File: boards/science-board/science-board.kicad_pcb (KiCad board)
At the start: 2 copper layers, 93.2 x 93.2 mm, 19 parts, among them J1 Conn_01x02, J10 Conn_01x04, J11 J00-0045NL, J12 Conn_02x03_Counter_Clockwise, J2 Conn_01x08, J3 Conn_01x04, J4 Conn_01x04, J5 Conn_01x08, J6 Conn_01x03, J7 Conn_01x08, J8 Conn_01x08, J9 Conn_01x04, U1 Teensy4.1, U2 LSF0108PWR

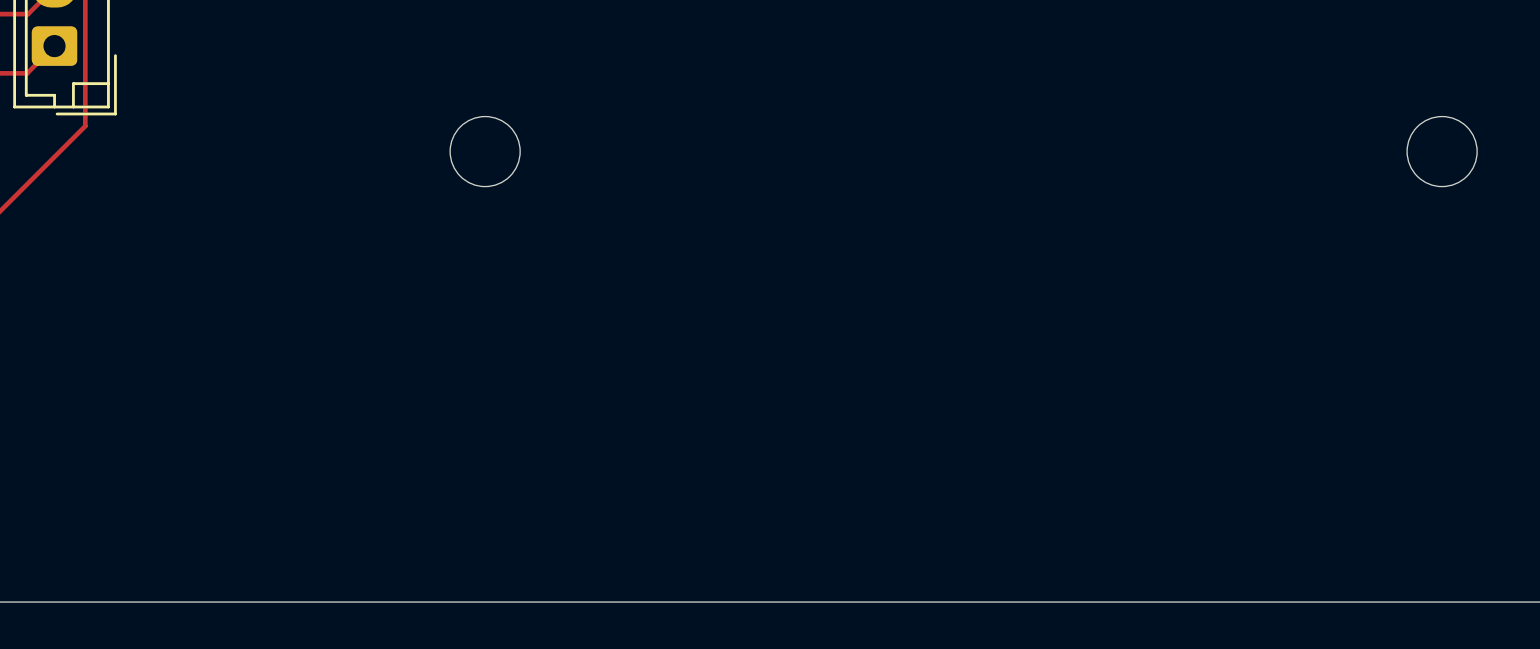
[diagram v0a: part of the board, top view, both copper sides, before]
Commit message: Added logo to science board
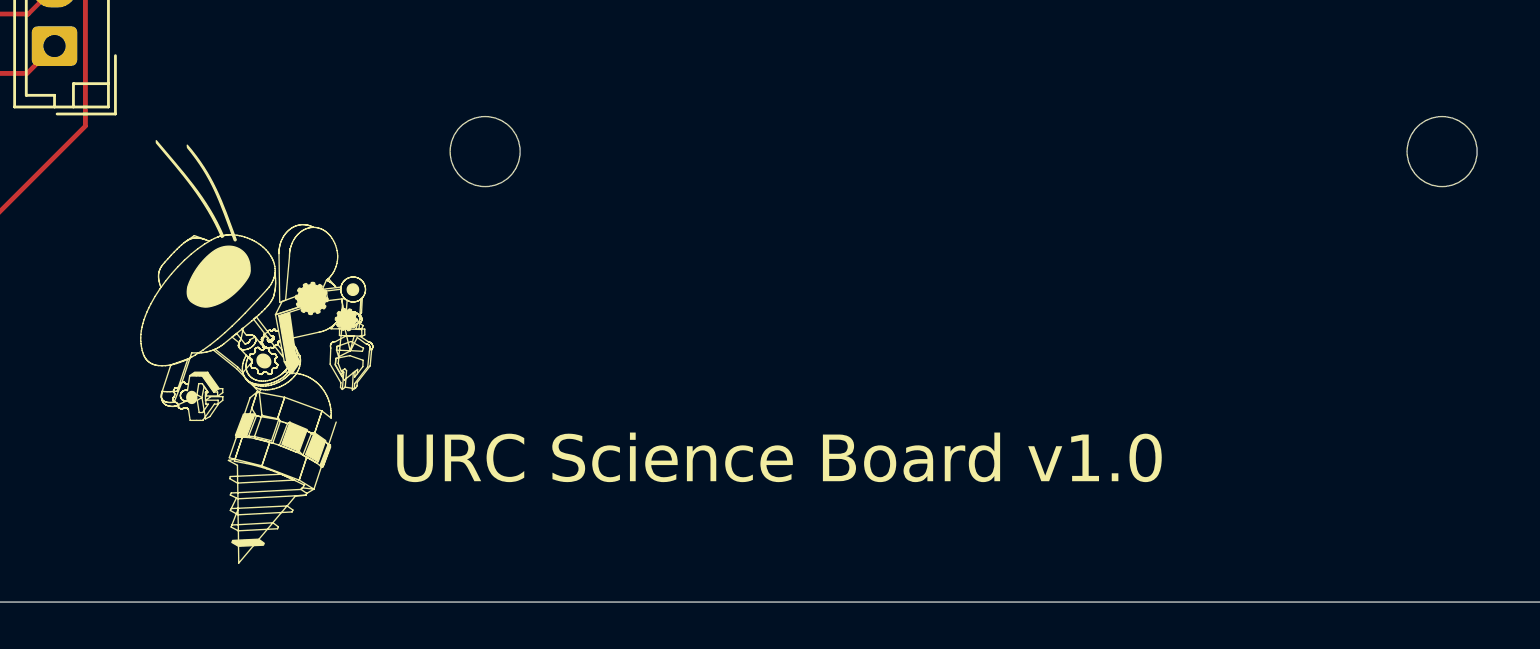
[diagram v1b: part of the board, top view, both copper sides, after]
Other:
- board text added: "URC Science Board v1.0"

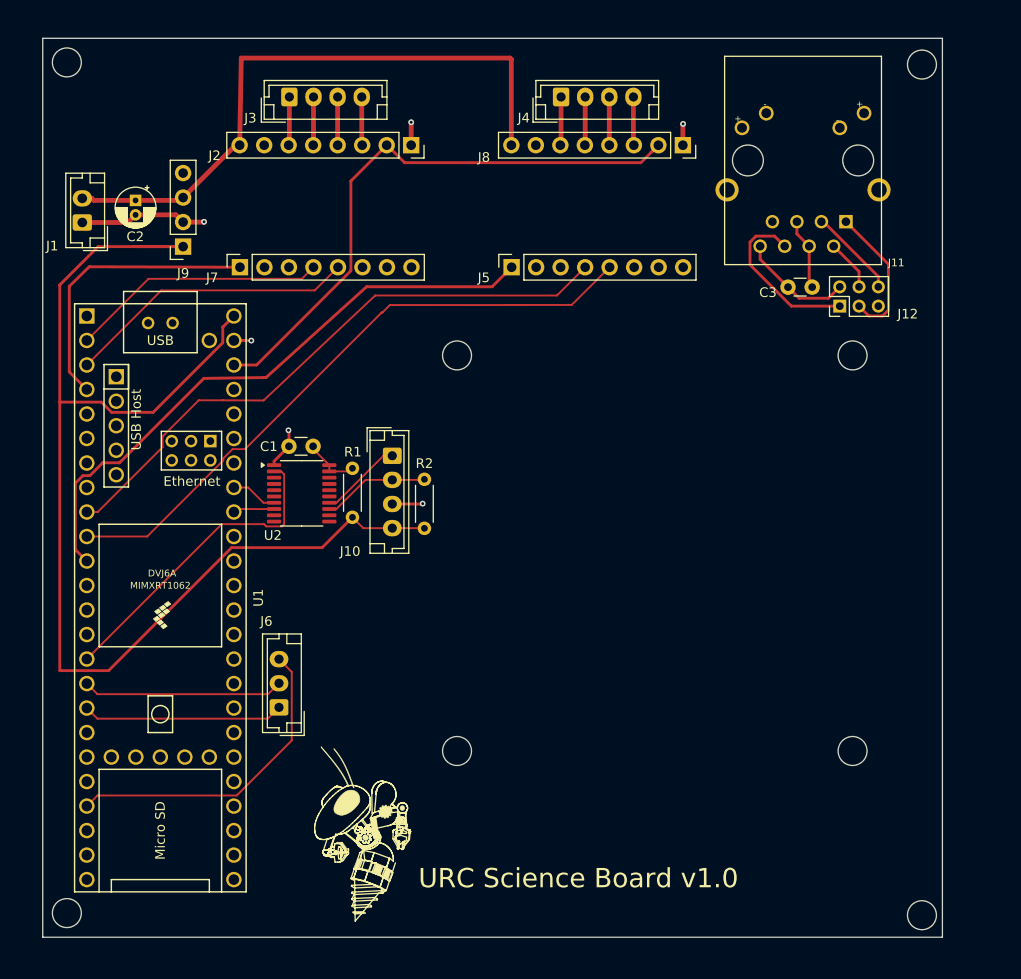
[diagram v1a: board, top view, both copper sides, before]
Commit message: updated science board-GND
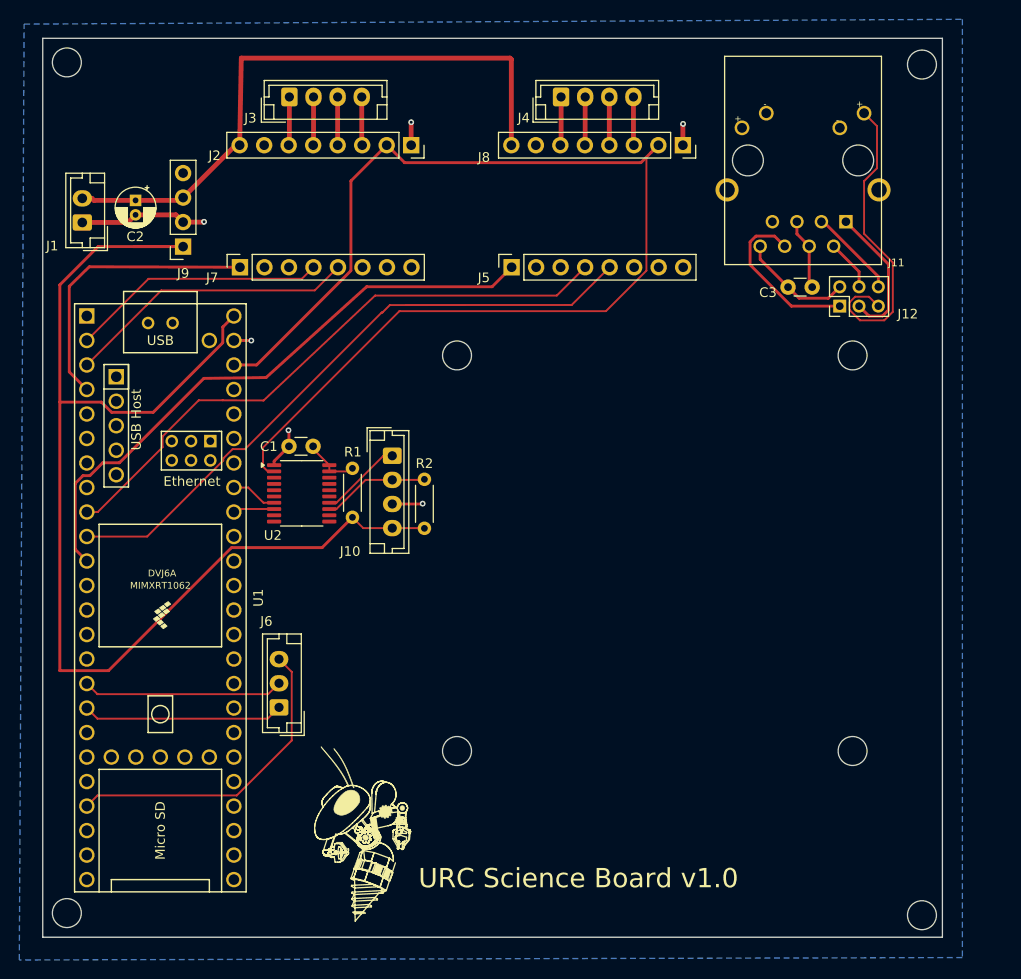
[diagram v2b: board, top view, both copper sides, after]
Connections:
- U1 pad 15: +3.3V -> unconnected-(U1-3V3-Pad15)
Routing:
- net /LED: track 0.00 -> 32.6 mm
- net +3.3V: track 94.3 -> 125.8 mm
- added copper zone on B.Cu, net GND

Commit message: Changes to Science and Arm Board
Added pin labels to both boards
Fixed Mislabeled Stepper Board Footprint in Arm board
Added extra digital pins and ground in Science Board
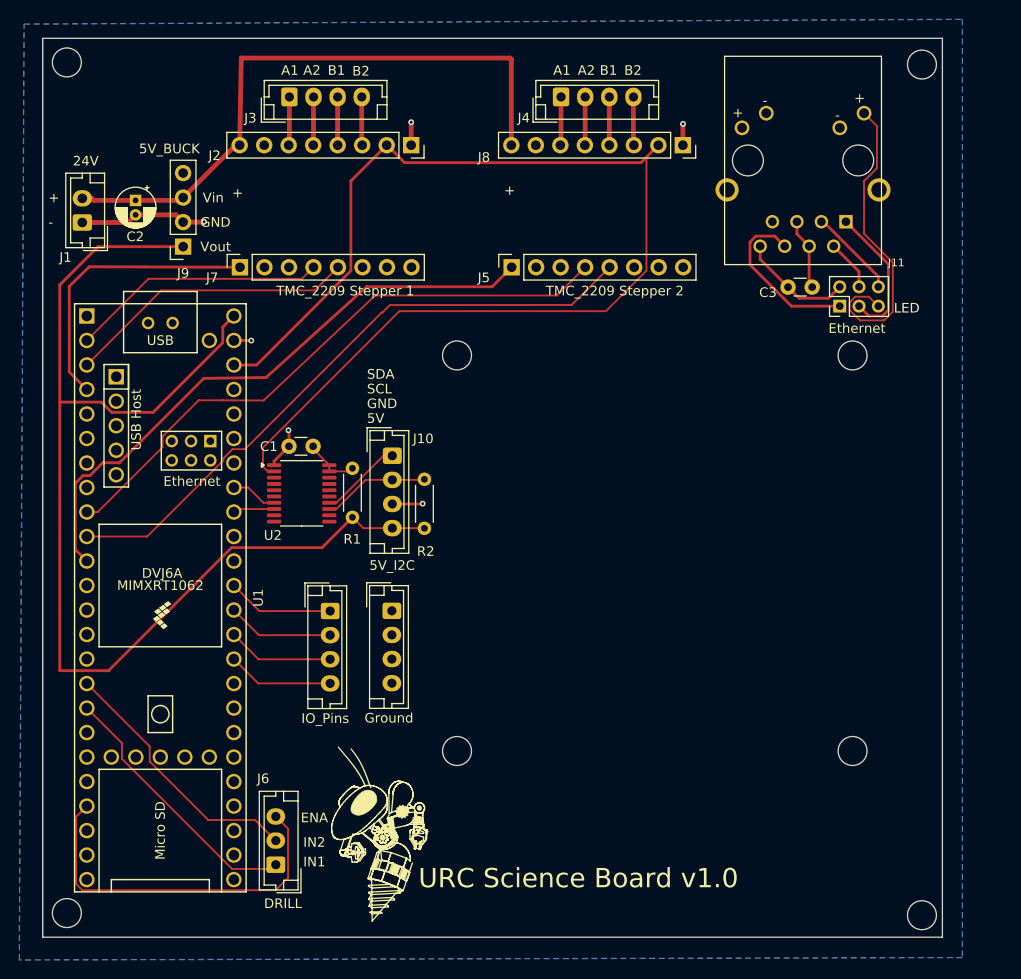
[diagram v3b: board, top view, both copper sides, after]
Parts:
- added Ground: Conn_01x04, Connector_JST:JST_EH_B4B-EH-A_1x04_P2.50mm_Vertical, F.Cu at (52.1, 79.6)
- added IO_Pins: Conn_01x04, Connector_JST:JST_EH_B4B-EH-A_1x04_P2.50mm_Vertical, F.Cu at (45.7, 79.6)
- moved J6 16.3 mm to (40.1, 105.9)
- renumbered J12 to Ethernet
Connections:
- U1 pad 34: unconnected-(U1-GND-Pad34) -> /34
- U1 pad 35: unconnected-(U1-13_SCK_LED-Pad35) -> /35
- U1 pad 36: unconnected-(U1-14_A0_TX3_SPDIF_OUT-Pad36) -> /36
- U1 pad 37: unconnected-(U1-15_A1_RX3_SPDIF_IN-Pad37) -> /37
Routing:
- net /37: track 0.00 -> 11.1 mm
- net /36: track 0.00 -> 11.1 mm
- net /35: track 0.00 -> 11.0 mm
- net /34: track 0.00 -> 11.0 mm
- net /EN1: track 20.9 -> 27.6 mm
- net /EN2: track 20.8 -> 27.2 mm
- net /ENA: track 33.0 -> 38.2 mm
- net +5V: track 127.9 -> 122.8 mm
- net +3.3V: track 125.8 -> 122.9 mm
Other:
- board text added: "+"
- board text added: "-"
- board text added: "24V"
- board text added: "5V"
- board text added: "5V_BUCK"
- board text added: "5V_I2C"
- board text added: "A1"
- board text added: "A2"
- board text added: "B1"
- board text added: "B2"
- board text added: "DRILL"
- board text added: "ENA"
- board text added: "GND"
- board text added: "IN1"
- board text added: "IN2"
- board text added: "LED"
- board text added: "SCL"
- board text added: "SDA"
- board text added: "TMC_2209 Stepper 1"
- board text added: "TMC_2209 Stepper 2"
- board text added: "Vin"
- board text added: "Vout"

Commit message: Removed I2C level converter from Science Board
BRUH
The temperature probe works running on 3.3V so the level converter for I2C wasn't even necessary on the Science Board. I have removed it from the schematic and updated the PCB layout.
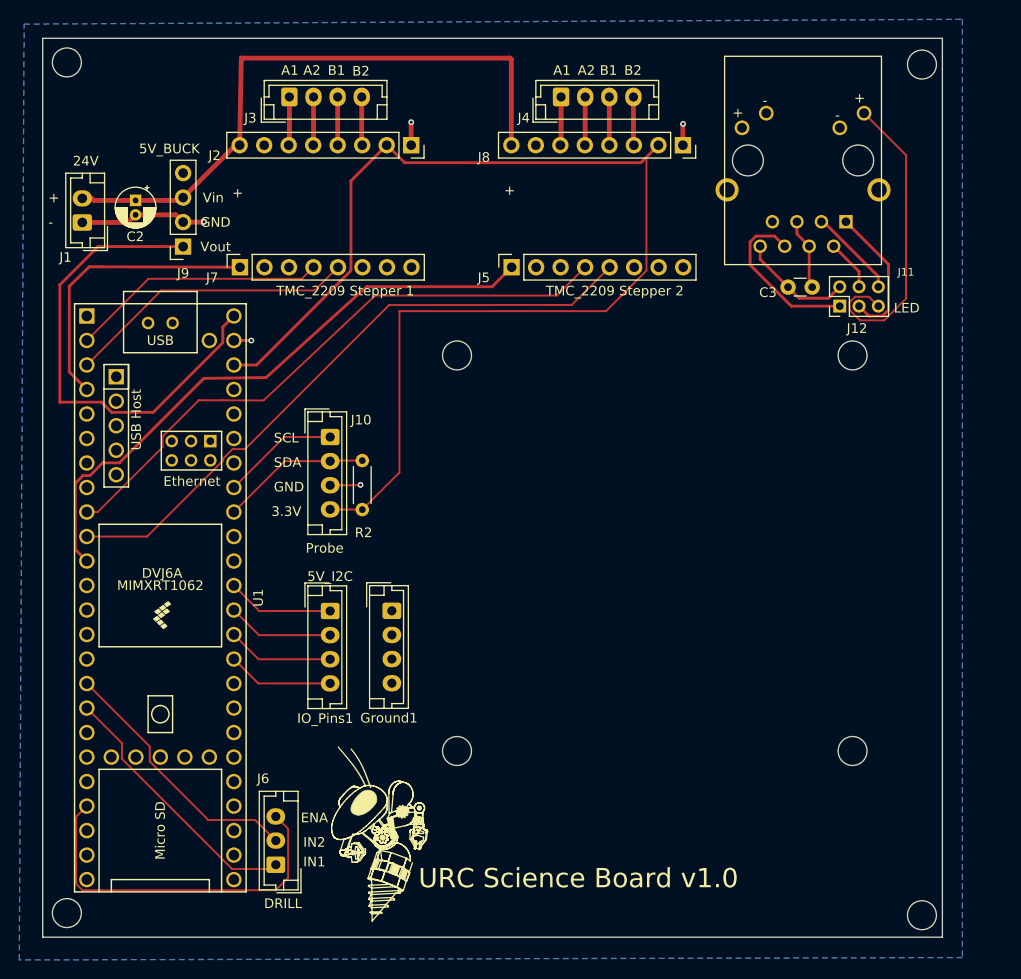
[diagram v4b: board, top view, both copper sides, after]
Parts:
- removed C1: 0.1uF, Capacitor_THT:C_Disc_D3.0mm_W1.6mm_P2.50mm
- removed R1: 200k, Resistor_THT:R_Axial_DIN0204_L3.6mm_D1.6mm_P5.08mm_Horizontal
- removed U2: LSF0108PWR, Package_SO:TSSOP-20_4.4x6.5mm_P0.65mm
- moved R2 6.73 mm to (49.0, 64.0)
- moved J10 6.73 mm to (45.7, 61.5)
- renumbered Ground to Ground1, IO_Pins to IO_Pins1, Ethernet to J12
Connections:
- J10 pad 1: /Yellow/SCL -> SCL
- J10 pad 2: /Black/SDA -> SDA
- J10 pad 4: +5V -> +3.3V
- R2 pad 1: /Black/SDA -> SDA
- R2 pad 2: +5V -> +3.3V
- U1 pad 40: TEMP_SDA -> SDA
- U1 pad 41: TEMP_SCL -> SCL
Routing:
- net +5V: track 122.8 -> 50.1 mm
- net SDA: track 0.00 -> 15.5 mm
- net SCL: track 0.00 -> 12.1 mm
- net /Black/SDA: track 11.1 -> 0.00 mm
- net /Yellow/SCL: track 8.54 -> 0.00 mm
- net /EN: track 5.83 -> 0.00 mm
- net TEMP_SCL: track 4.82 -> 0.00 mm
- net TEMP_SDA: track 4.30 -> 0.00 mm
- net GND: track 38.9 -> 34.6 mm, vias 6 -> 5
- net +3.3V: track 122.9 -> 125.1 mm
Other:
- board text added: "3.3V"
- board text added: "Probe"
- board text removed: "5V"

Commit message: Prepared Boards for PCB Manufacture
Added GND line for IMU on Main Board
Fixed Silkscreen Text Size for PCB Manufacture on Science, Main, and Arm boards
Generated Gerber Files for Science, Main, and Arm boards
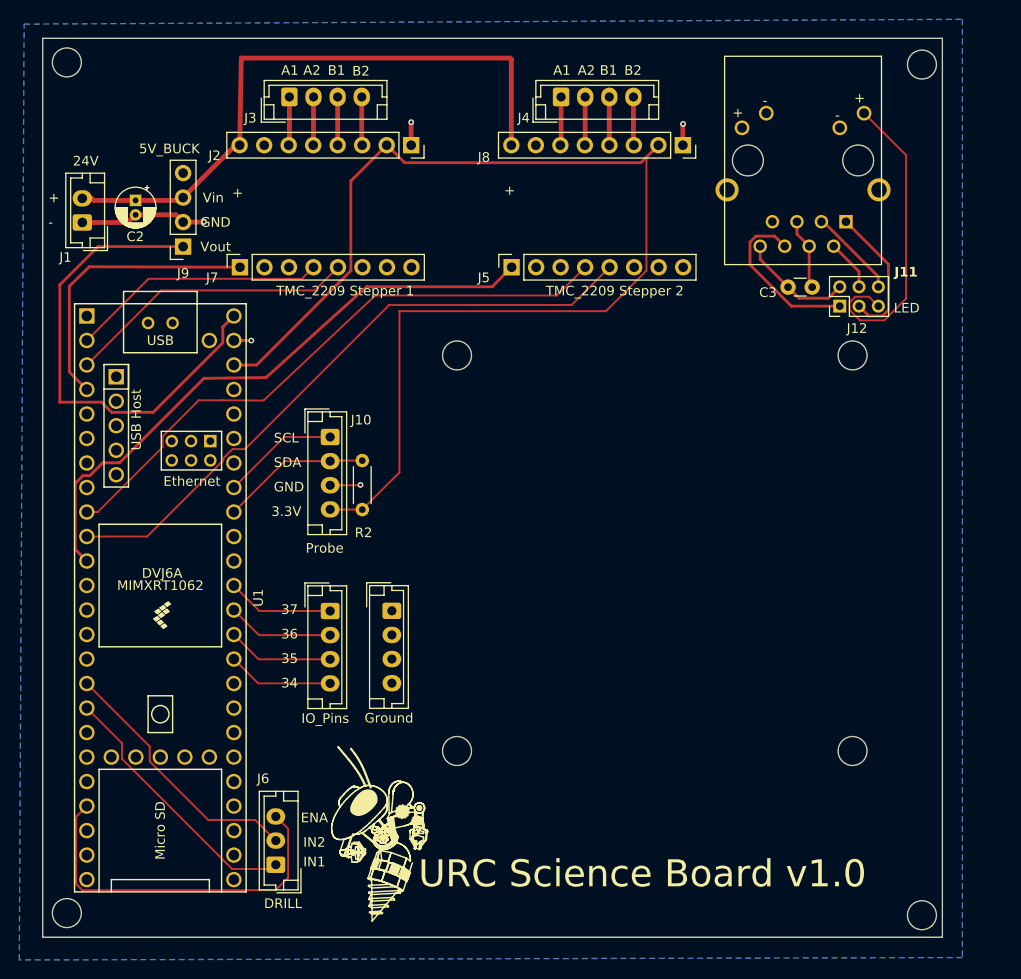
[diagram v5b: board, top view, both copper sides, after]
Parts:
- renumbered Ground1 to Ground, IO_Pins1 to IO_Pins
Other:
- board text added: "34"
- board text added: "35"
- board text added: "36"
- board text added: "37"
- board text removed: "5V_I2C"
